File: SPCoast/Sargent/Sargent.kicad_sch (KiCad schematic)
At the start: 43 parts, among them SW1 835, SW2 835, SW3 1, SW835 835

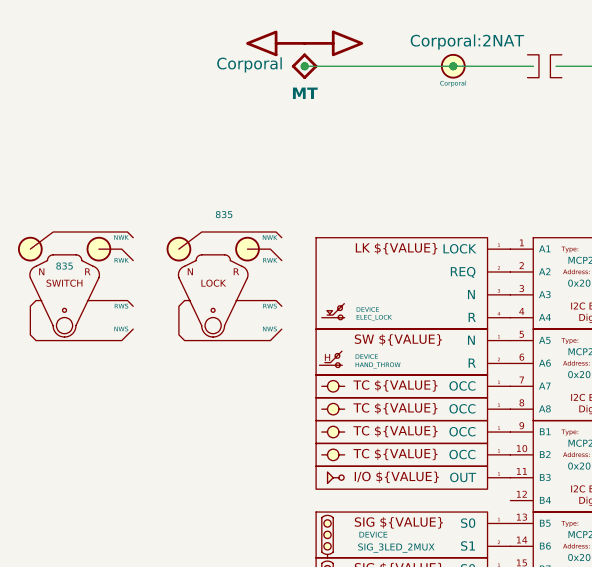
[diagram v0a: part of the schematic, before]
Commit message: chore(kicad): refresh instances to the ADR 0003 libraries (InterlockingPlant 95f53e2)
- Desk sheets (South-cTc/*) and the Sargent sandbox: embedded PanelSwitch, PanelLock,
  PanelSignal, PanelMCall, PanelCode, PanelLamp-*, PanelColumn-MAX7313 definitions refreshed
  from the library (refresh_embedded.py, checked against the pre-pass library: only Description
  text had drifted). Instance Role APPLIANCE -> PANEL (77).
- Plant sheets: powered-switch instance Kind SWITCH_POWERED -> SWITCH_REMOTE (21), matching the
  library (sweep_role_kind_fields.py).

Verified:
- verify_symbol_diff.py: same symbols, lib_ids and positions; only Role/Kind changed.
- Nets unchanged: Christopher 30, Corporal 27, GilroyCalTrain 28, GilroyInterchange 23,
  Luchessa 35, Sargent 61, Watsonville 99, South-cTc 341.
- parse_kicad_plant.py --format text identical before/after for all seven plants.
- Desk compile 75/137/14, diagnostics identical; the 7 desk locks bind WLS/~{WLS}/~{WLK}/WLK
  to the bits that were NWS/RWS/RWK/NWK.
- No sheet or project outside Luchessa carries the copied root UUID.

Co-Authored-By: Claude Opus 5.5 <noreply@anthropic.com>
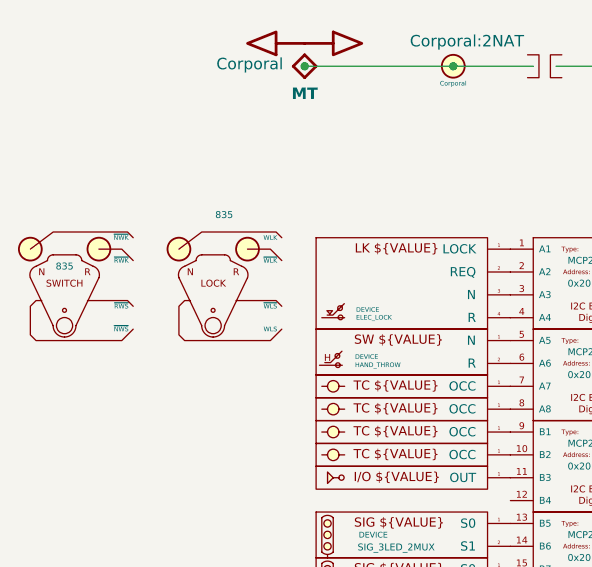
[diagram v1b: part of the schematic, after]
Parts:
- SW1, SW2: Role APPLIANCE -> PANEL
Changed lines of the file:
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@@
 			)
 		)
-		(property "Role" "APPLIANCE"
+		(property "Role" "PANEL"
 			(at 36.195 87.63 0)
 			(hide yes)
@@
 			)
 		)
-		(property "Role" "APPLIANCE"
+		(property "Role" "PANEL"
 			(at 19.685 88.9 0)
 			(hide yes)

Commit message: chore(kicad): desk sheets to Driver-I2C-MAX7313 and the PanelLock Kind (InterlockingPlant owner review)
- 14 desk expanders: lib_id RailroadPanel:PanelColumn-MAX7313 -> Driver-I2C-MAX7313, embedded
  definition refreshed (pins A1..B8, same numbers and positions).
- 8 PanelLock instances: Kind LOCK_LEVER -> LOCK_LEVER_2LAMP_2CONTACT (7 desk, 1 Sargent sandbox).

Verified:
- verify_symbol_diff.py: only those lib_id and Kind changes.
- South-cTc 341 nets, Sargent 61; desk compile 75/137/14 with bindings identical to e2c1093.

Co-Authored-By: Claude Opus 5.5 <noreply@anthropic.com>
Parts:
- SW1: Kind LOCK_LEVER -> LOCK_LEVER_2LAMP_2CONTACT
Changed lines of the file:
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@@
 			)
 		)
-		(property "Kind" "LOCK_LEVER"
+		(property "Kind" "LOCK_LEVER_2LAMP_2CONTACT"
 			(at 36.195 85.725 0)
 			(hide yes)

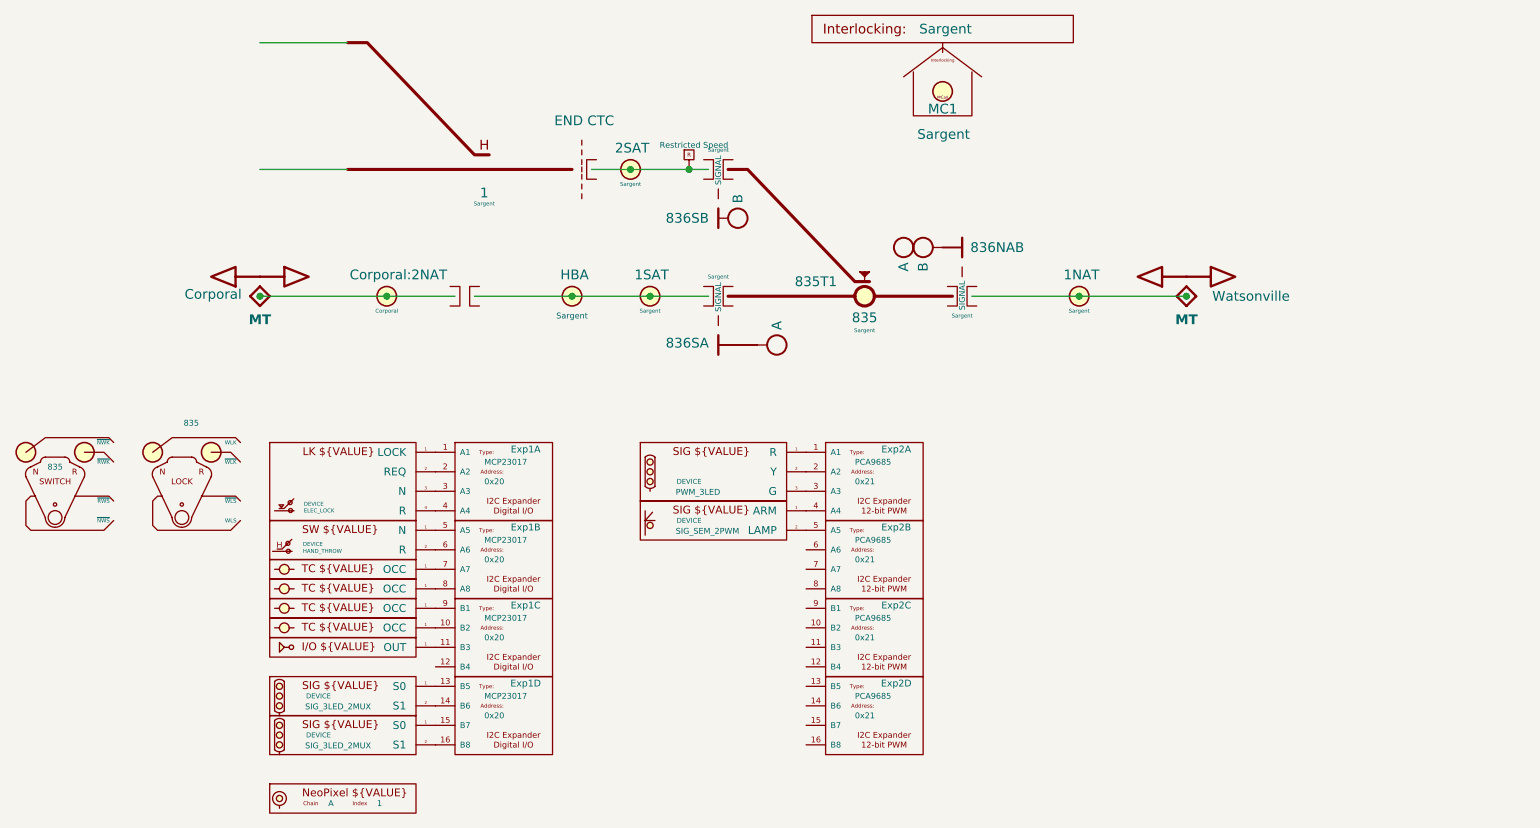
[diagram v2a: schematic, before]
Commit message: sandbox: Sargent fascia switches and lock plate (owner's edit, baseline)
Verified: committed as saved by the owner; no edits.

Co-Authored-By: Claude Opus 5.5 <noreply@anthropic.com>
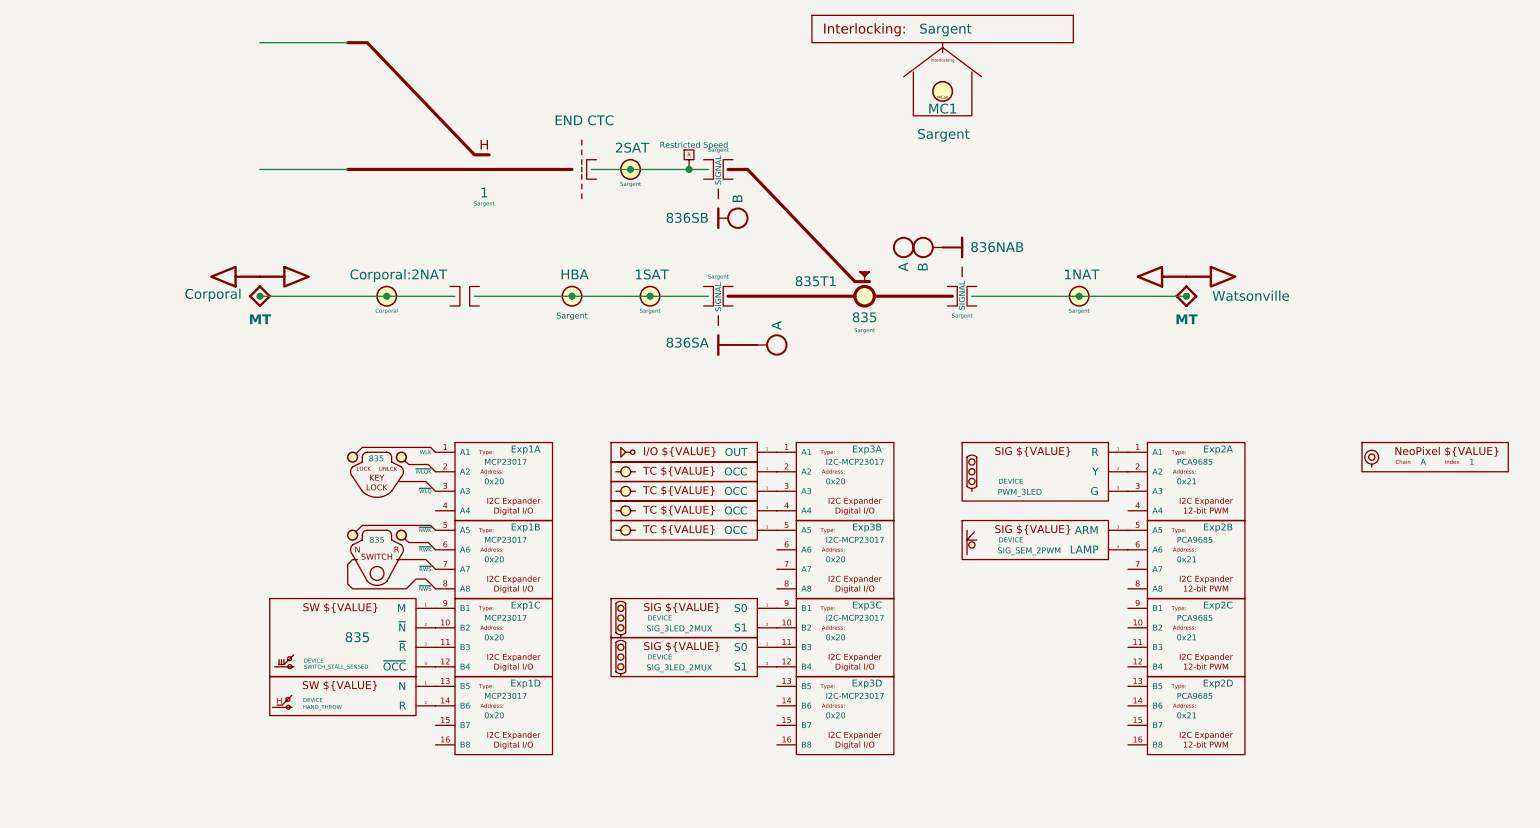
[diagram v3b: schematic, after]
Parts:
- removed DevSW1: 835, symbol RailroadField:Device-Switch-ElectricLock
- removed SW1: 835, symbol RailroadPanel:PanelLock
- removed SW2: 835, symbol RailroadPanel:PanelSwitch
- added DevSW1: 835, symbol RailroadField:Device-Switch-StallMotor-Sensed-OS
- added Exp3: ${ADDRESS}, symbol RailroadField:Driver-I2C-MCP23017
- added LK1: 835, symbol RailroadField:Local-Lock
- added SW1: 835, symbol RailroadField:Local-Switch
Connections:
- net at Exp1.5 (A5): now also SW1.4 (~{NWK}); no longer DevSW2.1 (N)
- net at Exp1.6 (A6): now also SW1.3 (~{RWK}); no longer DevSW2.2 (R)
- net at DevSW4.1 (S0): now also Exp3.9 (B1); no longer Exp1.13 (B5)
- net at DevSW4.2 (S1): now also Exp3.10 (B2); no longer Exp1.14 (B6)
- net at Exp1.7 (A7): now also SW1.2 (~{RWS}); no longer DevSW3.1 (OCC)
- net at Exp1.8 (A8): now also SW1.1 (~{NWS}); no longer DevSW8.1 (OCC)
- net at Exp2.5 (A5): now also DevSW7.1 (ARM); no longer DevSW7.2 (LAMP)
- net at Exp2.6 (A6): now also DevSW7.2 (LAMP)
- net at Exp1.10 (B2): now also DevSW1.2 (~{N}); no longer DevSW10.1 (OCC)
- net at DevSW12.1 (OUT): now also Exp3.1 (A1); no longer Exp1.11 (B3)
- net at Exp1.12 (B4): now also DevSW1.4 (~{OCC})
- net at DevSW9.1 (OCC): now also Exp3.4 (A4); no longer Exp1.9 (B1)
- net at Exp1.1 (A1): now also LK1.3 (WLK)
- net at Exp1.2 (A2): now also LK1.2 (~{WLQK})
- net at Exp1.3 (A3): now also LK1.1 (~{WLQ})
- net at DevSW5.1 (S0): now also Exp3.11 (B3); no longer Exp1.15 (B7)
- net at DevSW5.2 (S1): now also Exp3.12 (B4); no longer Exp1.16 (B8)
- net at Exp2.4 (A4): no longer DevSW7.1 (ARM)
- new net: DevSW3.1 (OCC), Exp3.2 (A2)
- new net: DevSW8.1 (OCC), Exp3.3 (A3)
- new net: DevSW1.3 (~{R}), Exp1.11 (B3)
- new net: DevSW1.1 (M), Exp1.9 (B1)
- new net: DevSW10.1 (OCC), Exp3.5 (A5)
- new net: DevSW2.1 (N), Exp1.13 (B5)
- new net: DevSW2.2 (R), Exp1.14 (B6)
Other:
- moved on the sheet: Exp2A, Exp2B, Exp2C, Exp2D

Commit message: sandbox: Sargent Exp3 address and 835 OS detector fixed (owner's edit, baseline)
Verified: committed as saved; no edits.

Co-Authored-By: Claude Opus 5.5 <noreply@anthropic.com>
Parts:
- removed DevSW3: 835T1, symbol RailroadField:Device-TrackCircuit
- Exp2: Address 0x21 -> 0x27
- Exp3: Address 0x20 -> 0x21
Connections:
- net at Exp3.4 (A4): now also DevSW10.1 (OCC); no longer DevSW9.1 (OCC)
- net at Exp3.2 (A2): now also DevSW8.1 (OCC)
- net at Exp3.3 (A3): now also DevSW9.1 (OCC); no longer DevSW8.1 (OCC)
- net at DevSW4.2 (S1): now also Exp3.6 (A6); no longer Exp3.10 (B2)
- net at DevSW5.1 (S0): now also Exp3.7 (A7); no longer Exp3.11 (B3)
- net at DevSW5.2 (S1): now also Exp3.8 (A8); no longer Exp3.12 (B4)
- net at DevSW4.1 (S0): now also Exp3.5 (A5); no longer Exp3.9 (B1)

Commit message: sandbox: Sargent to the ADR 0003/0004 field libraries (pass 3)
Scripted (FieldUnit-Subdivision docs/review/handoff-field-io-cleanup/pass3_sargent.py) over the
owner's baseline. lib_ids and embedded definitions: Device-I2C-IOx4/-PWMx4 -> Driver-I2C-MCP23017/
-PCA9685; Device-TrackCircuit -> Device-Detector-Optical; Device-Digital_Output -> Device-Lamp-Bit
(MC1); Device-Signal-1LED_NEO -> Device-Lamp-NeoPixel (HBA, an auxiliary); Device-Signal-* ->
Device-Head-*; Device-Switch-HandThrow -> Device-Switch-Sense (1); plant Switch_HandThrow ->
Switch_Manual_Sensed (1, outside the END_CTC limit). Instance Role/Kind refreshed; Polarity dropped.

Verified:
- Every mapping has identical pin numbers and positions; netlist connectivity identical (67 nets).
- verify_symbol_diff.py: no symbol added, removed or moved.
- parse_kicad_plant.py --format text: only names change (40 -> 39 errors; the field symbols and
  Switch_Manual_Sensed are unknown to the plant compiler until #30 step 3).
- field_resolve.py: every device resolves to a plant item, one driver pin each, none shared,
  addresses unique.

Co-Authored-By: Claude Opus 5.5 <noreply@anthropic.com>
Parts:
- DevSW10, DevSW8, DevSW9: symbol RailroadField:Device-TrackCircuit -> RailroadField:Device-Detector-Optical; Kind TRACK_CIRCUIT -> DETECTOR_OPTICAL; Polarity !OCC -> (none)
- DevSW12: symbol RailroadField:Device-Digital_Output -> RailroadField:Device-Lamp-Bit; Kind DIGITAL_OUTPUT -> LAMP_BIT; Polarity OUT -> (none)
- DevSW13: symbol RailroadField:Device-Signal-1LED_NEO -> RailroadField:Device-Lamp-NeoPixel; Kind SIG_1LED_NEOPIXEL -> LAMP_NEOPIXEL
- DevSW2: symbol RailroadField:Device-Switch-HandThrow -> RailroadField:Device-Switch-Sense; Kind HAND_THROW -> SWITCH_SENSE; Polarity N,R -> (none)
- DevSW4, DevSW5: symbol RailroadField:Device-Signal-3LED_2MUX -> RailroadField:Device-Head-3LED-Mux2; Kind SIG_3LED_2MUX -> HEAD_3LED_MUX2
- DevSW6: symbol RailroadField:Device-Signal-3LED_PWM -> RailroadField:Device-Head-3LED-PWM; Kind PWM_3LED -> HEAD_3LED_PWM
- DevSW7: symbol RailroadField:Device-Signal-Semaphore_2PWM -> RailroadField:Device-Head-Semaphore-Servo; Kind SIG_SEM_2PWM -> HEAD_SEMAPHORE_SERVO
- Exp1: symbol RailroadField:Device-I2C-IOx4 -> RailroadField:Driver-I2C-MCP23017; Kind MCP23017 -> I2C-MCP23017; Role IODriver -> IODRIVER
- Exp2: symbol RailroadField:Device-I2C-PWMx4 -> RailroadField:Driver-I2C-PCA9685; Kind PCA9685 -> I2C-PCA9685; Role IODriver -> IODRIVER
- SW3: symbol Railroad:Switch_HandThrow -> Railroad:Switch_Manual_Sensed; Kind SWITCH_MANUAL -> SWITCH_MANUAL_SENSED
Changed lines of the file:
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@@
 	)
 	(symbol
-		(lib_id "RailroadField:Device-Signal-3LED_2MUX")
+		(lib_id "RailroadField:Device-Head-3LED-Mux2")
 		(at 102.87 83.82 0)
 		(unit 1)
@@
 			)
 		)
-		(property "Kind" "SIG_3LED_2MUX"
+		(property "Kind" "HEAD_3LED_MUX2"
 			(at 96.0471 85.1912 0)
 			(show_name no)
@@
 	)
 	(symbol
-		(lib_id "Railroad:Switch_HandThrow")
+		(lib_id "Railroad:Switch_Manual_Sensed")
 		(at 74.93 35.56 0)
 		(mirror y)
@@
 			)
 		)
-		(property "Kind" "SWITCH_MANUAL"
+		(property "Kind" "SWITCH_MANUAL_SENSED"
 			(at 74.93 35.56 0)
 			(hide yes)
@@
 	)
 	(symbol
-		(lib_id "RailroadField:Device-TrackCircuit")
+		(lib_id "RailroadField:Device-Detector-Optical")
 		(at 102.87 80.01 0)
 		(unit 1)
@@
 			)
 		)
-		(property "Kind" "TRACK_CIRCUIT"
+		(property "Kind" "DETECTOR_OPTICAL"
 			(at 103.3691 78.0651 0)
 			(hide yes)
@@
 			)
 		)
-		(property "Polarity" "!OCC"
-			(at 97.79 76.2 0)
-			(hide yes)
-			(show_name no)
-			(do_not_autoplace no)
-			(effects
-				(font
-					(size 1.27 1.27)
-				)
-			)
-		)
 		(pin "1"
 		)
@@
 	)
 	(symbol
-		(lib_id "RailroadField:Device-I2C-IOx4")
+		(lib_id "RailroadField:Driver-I2C-MCP23017")
 		(at 68.58 82.55 0)
 		(unit 2)
@@
 			)
 		)
-		(property "Role" "IODriver"
+		(property "Role" "IODRIVER"
 			(at 63.5 80.01 0)
 			(hide yes)
@@
 			)
 		)
-		(property "Kind" "MCP23017"
+		(property "Kind" "I2C-MCP23017"
 			(at 74.93 83.82 0)
 			(show_name no)
@@
 	)
 	(symbol
-		(lib_id "RailroadField:Device-I2C-PWMx4")
+		(lib_id "RailroadField:Driver-I2C-PCA9685")
 		(at 158.75 82.55 0)
 		(unit 2)
@@
 			)
 		)
-		(property "Role" "IODriver"
+		(property "Role" "IODRIVER"
 			(at 153.67 80.01 0)
 			(hide yes)
@@
 			)
 		)
-		(property "Kind" "PCA9685"
+		(property "Kind" "I2C-PCA9685"
 			(at 165.1 83.82 0)
 			(show_name no)
@@
 	)
 	(symbol
-		(lib_id "RailroadField:Device-Signal-3LED_2MUX")
+		(lib_id "RailroadField:Device-Head-3LED-Mux2")
 		(at 102.87 88.9 0)
 		(unit 1)
@@
 			)
 		)
-		(property "Kind" "SIG_3LED_2MUX"
+		(property "Kind" "HEAD_3LED_MUX2"
 			(at 96.0471 90.2712 0)
 			(show_name no)
@@
 	)
 	(symbol
-		(lib_id "RailroadField:Device-TrackCircuit")
+		(lib_id "RailroadField:Device-Detector-Optical")
 		(at 102.87 77.47 0)
 		(unit 1)
@@
 			)
 		)
-		(property "Kind" "TRACK_CIRCUIT"
+		(property "Kind" "DETECTOR_OPTICAL"
 			(at 103.3691 75.5251 0)
 			(hide yes)
@@
 			)
 		)
-		(property "Polarity" "!OCC"
-			(at 97.79 73.66 0)
-			(hide yes)
-			(show_name no)
-			(do_not_autoplace no)
-			(effects
-				(font
-					(size 1.27 1.27)
-				)
-			)
-		)
 		(pin "1"
 		)
@@
 	)
 	(symbol
-		(lib_id "RailroadField:Device-I2C-IOx4")
+		(lib_id "RailroadField:Driver-I2C-MCP23017")
 		(at 68.58 92.71 0)
 		(unit 3)
@@
 			)
 		)
-		(property "Role" "IODriver"
+		(property "Role" "IODRIVER"
 			(at 63.5 90.17 0)
 			(hide yes)
@@
 			)
 		)
-		(property "Kind" "MCP23017"
+		(property "Kind" "I2C-MCP23017"
 			(at 74.93 93.98 0)
 			(show_name no)
@@
 	)
 	(symbol
-		(lib_id "RailroadField:Device-I2C-IOx4")
+		(lib_id "RailroadField:Driver-I2C-MCP23017")
 		(at 68.58 72.39 0)
 		(unit 1)
@@
 			)
 		)
-		(property "Role" "IODriver"
+		(property "Role" "IODRIVER"
 			(at 63.5 69.85 0)
 			(hide yes)
@@
 			)
 		)
-		(property "Kind" "MCP23017"
+		(property "Kind" "I2C-MCP23017"
 			(at 74.93 73.66 0)
 			(show_name no)
@@
 	)
 	(symbol
-		(lib_id "RailroadField:Device-TrackCircuit")
+		(lib_id "RailroadField:Device-Detector-Optical")
 		(at 102.87 74.93 0)
 		(unit 1)
@@
 			)
 		)
-		(property "Kind" "TRACK_CIRCUIT"
+		(property "Kind" "DETECTOR_OPTICAL"
 			(at 103.3691 72.9851 0)
 			(hide yes)
@@
 			)
 		)
-		(property "Polarity" "!OCC"
-			(at 97.79 71.12 0)
-			(hide yes)
-			(show_name no)
-			(do_not_autoplace no)
-			(effects
-				(font
-					(size 1.27 1.27)
-				)
-			)
-		)
 		(pin "1"
 		)
@@
 	)
 	(symbol
-		(lib_id "RailroadField:Device-I2C-IOx4")
+		(lib_id "RailroadField:Driver-I2C-MCP23017")
 		(at 68.58 102.87 0)
 		(unit 4)
@@
 			)
 		)
-		(property "Role" "IODriver"
+		(property "Role" "IODRIVER"
 			(at 63.5 100.33 0)
 			(hide yes)
@@
 			)
 		)
-		(property "Kind" "MCP23017"
+		(property "Kind" "I2C-MCP23017"
 			(at 74.93 104.14 0)
 			(show_name no)
@@
 	)
 	(symbol
-		(lib_id "RailroadField:Device-Signal-3LED_PWM")
+		(lib_id "RailroadField:Device-Head-3LED-PWM")
 		(at 148.59 73.66 0)
 		(unit 1)
@@
 			)
 		)
-		(property "Kind" "PWM_3LED"
+		(property "Kind" "HEAD_3LED_PWM"
 			(at 141.7671 77.5712 0)
 			(show_name no)
@@
 	)
 	(symbol
-		(lib_id "RailroadField:Device-Digital_Output")
+		(lib_id "RailroadField:Device-Lamp-Bit")
 		(at 102.87 72.39 0)
 		(unit 1)
@@
 			)
 		)
-		(property "Kind" "DIGITAL_OUTPUT"
+		(property "Kind" "LAMP_BIT"
 			(at 103.3691 70.4451 0)
 			(hide yes)
@@
 			)
 		)
-		(property "Polarity" "OUT"
-			(at 97.79 68.58 0)
-			(hide yes)
-			(show_name no)
-			(do_not_autoplace no)
-			(effects
-				(font
-					(size 1.27 1.27)
-				)
-			)
-		)
 		(pin "1"
 		)
@@
 	)
 	(symbol
-		(lib_id "RailroadField:Device-Signal-Semaphore_2PWM")
+		(lib_id "RailroadField:Device-Head-Semaphore-Servo")
 		(at 148.59 83.82 0)
 		(unit 1)
@@
 			)
 		)
-		(property "Kind" "SIG_SEM_2PWM"
+		(property "Kind" "HEAD_SEMAPHORE_SERVO"
 			(at 141.7671 85.1912 0)
 			(show_name no)
@@
 	)
 	(symbol
-		(lib_id "RailroadField:Device-I2C-PWMx4")
+		(lib_id "RailroadField:Driver-I2C-PCA9685")
 		(at 158.75 72.39 0)
 		(unit 1)
@@
 			)
 		)
-		(property "Role" "IODriver"
+		(property "Role" "IODRIVER"
 			(at 153.67 69.85 0)
 			(hide yes)
@@
 			)
 		)
-		(property "Kind" "PCA9685"
+		(property "Kind" "I2C-PCA9685"
 			(at 165.1 73.66 0)
 			(show_name no)
@@
 	)
 	(symbol
-		(lib_id "RailroadField:Device-I2C-PWMx4")
+		(lib_id "RailroadField:Driver-I2C-PCA9685")
 		(at 158.75 92.71 0)
 		(unit 3)
@@
 			)
 		)
-		(property "Role" "IODriver"
+		(property "Role" "IODRIVER"
 			(at 153.67 90.17 0)
 			(hide yes)
@@
 			)
 		)
-		(property "Kind" "PCA9685"
+		(property "Kind" "I2C-PCA9685"
 			(at 165.1 93.98 0)
 			(show_name no)
@@
 	)
 	(symbol
-		(lib_id "RailroadField:Device-Switch-HandThrow")
+		(lib_id "RailroadField:Device-Switch-Sense")
 		(at 58.42 104.14 0)
 		(unit 1)
@@
 			)
 		)
-		(property "Kind" "HAND_THROW"
+		(property "Kind" "SWITCH_SENSE"
 			(at 51.3116 105.5749 0)
 			(show_name no)
@@
 			)
 		)
-		(property "Polarity" "N,R"
-			(at 56.1141 100.972 0)
-			(hide yes)
-			(show_name no)
-			(do_not_autoplace no)
-			(effects
-				(font
-					(size 0.762 0.762)
-				)
-			)
-		)
 		(pin "2"
 		)
@@
 	)
 	(symbol
-		(lib_id "RailroadField:Device-I2C-PWMx4")
+		(lib_id "RailroadField:Driver-I2C-PCA9685")
 		(at 158.75 102.87 0)
 		(unit 4)
@@
 			)
 		)
-		(property "Role" "IODriver"
+		(property "Role" "IODRIVER"
 			(at 153.67 100.33 0)
 			(hide yes)
@@
 			)
 		)
-		(property "Kind" "PCA9685"
+		(property "Kind" "I2C-PCA9685"
 			(at 165.1 104.14 0)
 			(show_name no)
@@
 	)
 	(symbol
-		(lib_id "RailroadField:Device-Signal-1LED_NEO")
+		(lib_id "RailroadField:Device-Lamp-NeoPixel")
 		(at 200.66 73.66 0)
 		(unit 1)
@@
 			)
 		)
-		(property "Kind" "SIG_1LED_NEOPIXEL"
+		(property "Kind" "LAMP_NEOPIXEL"
 			(at 198.12 76.2 0)
 			(hide yes)
